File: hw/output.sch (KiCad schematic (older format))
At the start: 44 parts, among them J401 Conn_01x02, J402 Conn_01x02, J403 Conn_01x02, J404 Conn_01x02, J405 Conn_01x02, J406 Conn_01x02, J407 Conn_01x02, J408 Conn_01x02, J409 ServoCon, J410 AUDIO, Q401 IRLML6344TRPBF, Q402 IRLML6344TRPBF, Q403 IRLML6344TRPBF, Q404 CSD17306Q5A, Q406 IRLML6344TRPBF, Q408 CSD17306Q5A, U401 MCP1416, U402 MCP1416, U403 AD5160BRJZ10-R2, U404 MCP6001-OT, U405 TLP2361_TPL_E, U406 TLP2361_TPL_E

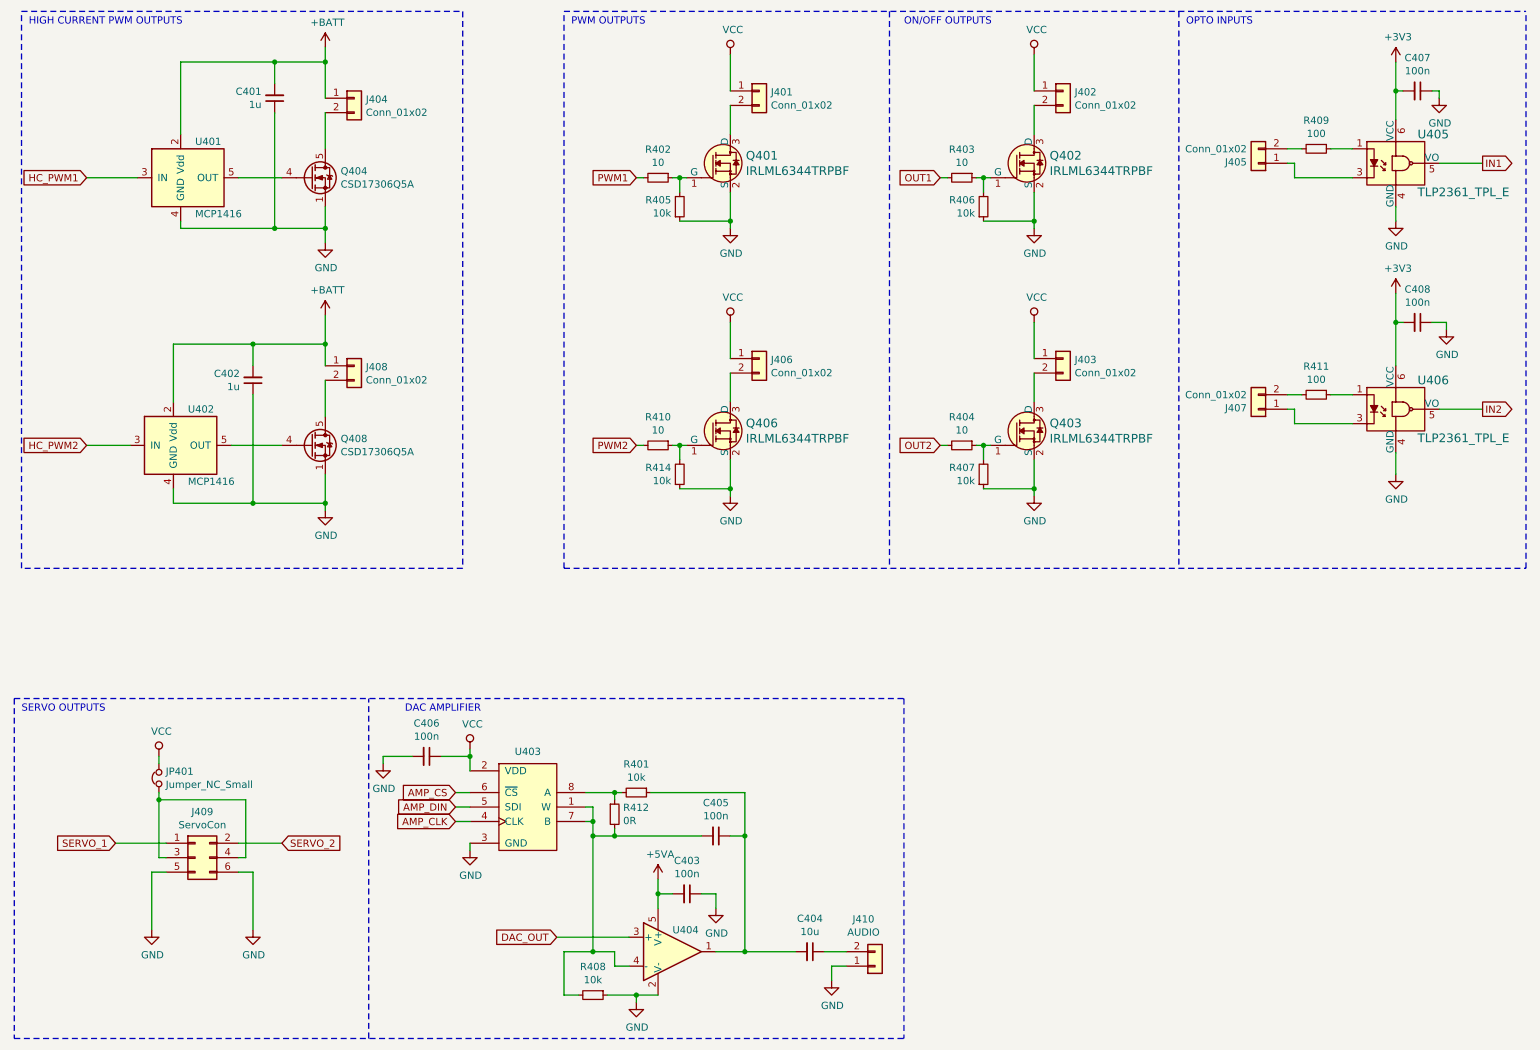
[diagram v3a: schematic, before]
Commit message: BOM Generation for 1.1 version
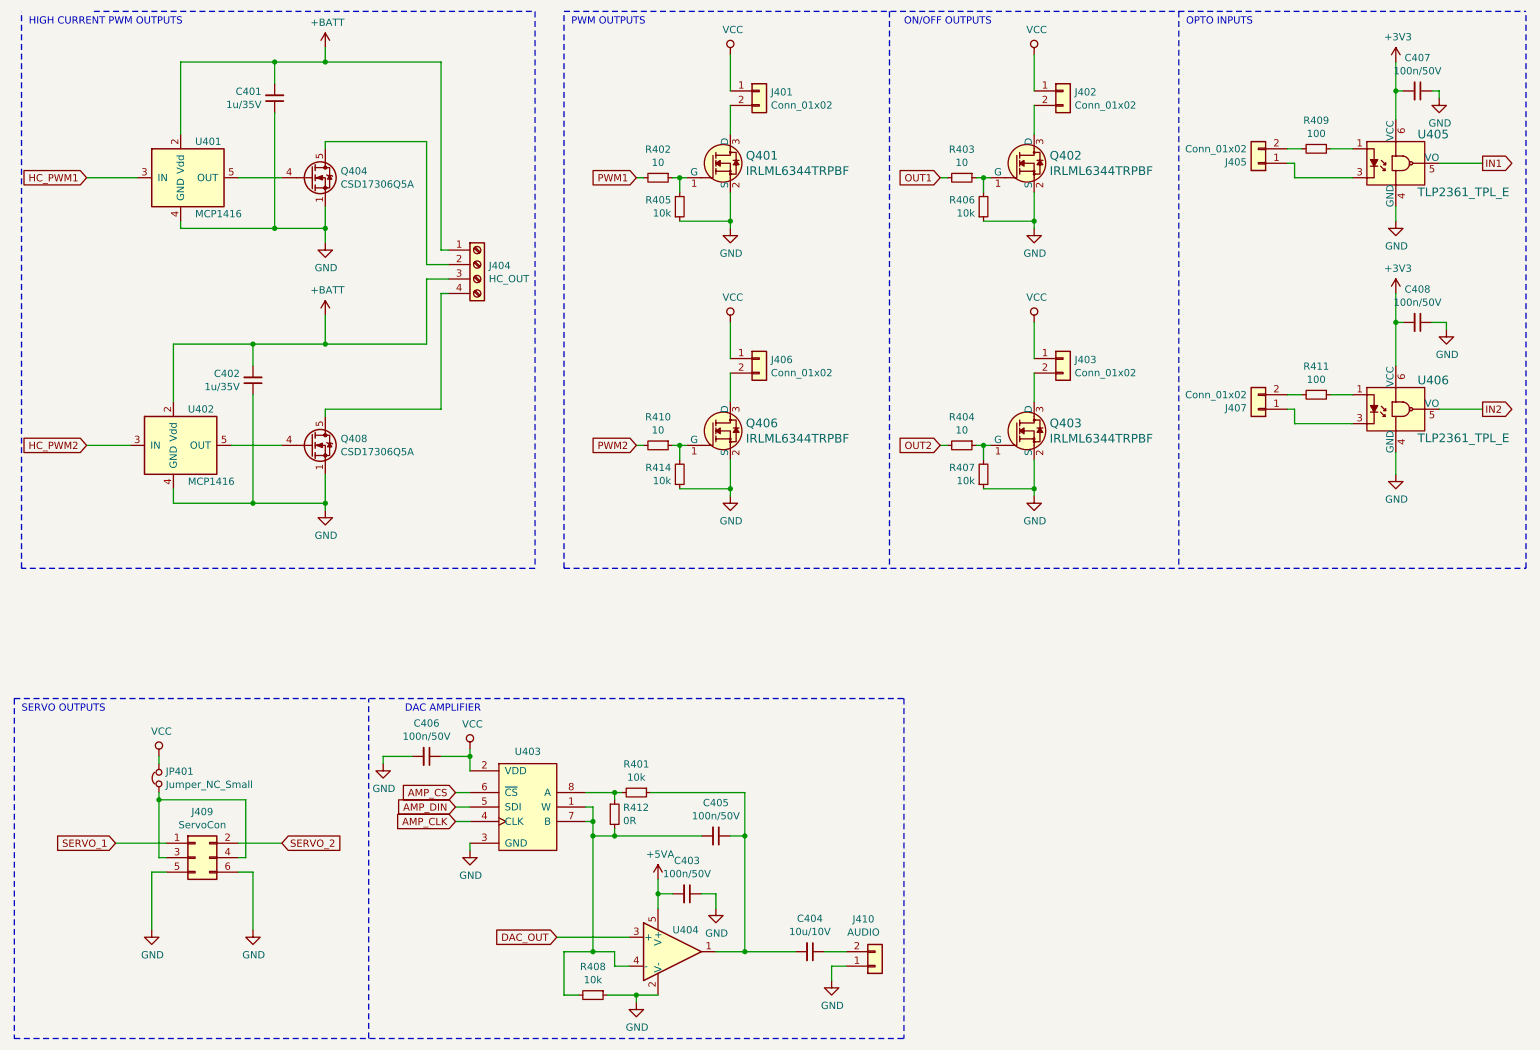
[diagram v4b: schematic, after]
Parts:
- removed J404, J408: Conn_01x02, TerminalBlock_Phoenix:TerminalBlock_Phoenix_PT-1,5-2-5.0-H_1x02_P5.00mm_Horizontal, symbol Connector_Generic:Conn_01x02
- added J404: HC_OUT, TerminalBlock_Phoenix:TerminalBlock_Phoenix_PT-1,5-4-5.0-H_1x04_P5.00mm_Horizontal, symbol Connector:Screw_Terminal_01x04
- C401, C402: value 1u -> 1u/35V
- C403, C405, C406, C407, C408: value 100n -> 100n/50V
- C404: value 10u -> 10u/10V
- J401, J402, J403, J405, J406, J407, J409, J410, JP401: Config (none) -> -prod
- Q404, Q408: MPN (none) -> CSD17306Q5A; Manufacturer (none) -> Texas Instruments
- R412: Config (none) -> dnp
- U401, U402: Description (none) -> Tiny 1.5A, High-Speed Power MOSFET DriverLo; MPN (none) -> MCP1416; Manufacturer (none) -> Microchip
- U403: Description (none) -> SPI Digital potentiometer 10k; MPN (none) -> Analog Devices; Manufacturer (none) -> AD5160BRJZ10-R2
- U404: MPN (none) -> MCP6001-OT; Manufacturer (none) -> Microchip
- U405, U406: MPN TLP2361(TPL,E -> TLP2361-TPLECT
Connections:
- net +BATT: now also J404.1 (Pin_1), J404.3 (Pin_3)
- net at Q404.5 (D): now also J404.2 (Pin_2)
- net at Q408.5 (D): now also J404.4 (Pin_4)
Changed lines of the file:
@@
 Sheet 4 4
 Title "RC Telemetry board"
-Date "2020-02-12"
-Rev "0.2"
+Date "2020-02-23"
+Rev "1.1"
 Comp "www.findersee.fi"
 Comment1 "https://github.com/findersee/rctelemetry"
@@
 	1    0    0    -1
 $EndComp
-$Comp
-L Connector_Generic:Conn_01x02 J404
-U 1 1 5CEA51F6
-P 2900 1250
-F 0 "J404" H 2980 1242 50  0000 L CNN
-F 1 "Conn_01x02" H 2980 1151 50  0000 L CNN
-F 2 "TerminalBlock_Phoenix:TerminalBlock_Phoenix_PT-1,5-2-5.0-H_1x02_P5.00mm_Horizontal" H 2900 1250 50  0001 C CNN
-F 3 "~" H 2900 1250 50  0001 C CNN
-	1    2900 1250
-	1    0    0    -1
-$EndComp
-Wire Wire Line
-	2700 1350 2700 1600
+Wire Wire Line
+	2700 1550 2700 1600
 $Comp
 L power:GND #PWR0408
@@
 	1    0    0    -1
 $EndComp
-$Comp
-L Connector_Generic:Conn_01x02 J408
-U 1 1 5CEA77CB
-P 2900 3100
-F 0 "J408" H 2980 3092 50  0000 L CNN
-F 1 "Conn_01x02" H 2980 3001 50  0000 L CNN
-F 2 "TerminalBlock_Phoenix:TerminalBlock_Phoenix_PT-1,5-2-5.0-H_1x02_P5.00mm_Horizontal" H 2900 3100 50  0001 C CNN
-F 3 "~" H 2900 3100 50  0001 C CNN
-	1    2900 3100
-	1    0    0    -1
-$EndComp
-Wire Wire Line
-	2700 3200 2700 3450
+Wire Wire Line
+	2700 3400 2700 3450
 $Comp
 L power:GND #PWR0416
@@
 F 2 "Connector_Molex:Molex_KK-254_AE-6410-02A_1x02_P2.54mm_Vertical" H 5700 1200 50  0001 C CNN
 F 3 "~" H 5700 1200 50  0001 C CNN
+F 4 "-prod" H 5700 1200 50  0001 C CNN "Config"
 	1    5700 1200
 	1    0    0    -1
@@
 F 2 "Connector_Molex:Molex_KK-254_AE-6410-02A_1x02_P2.54mm_Vertical" H 9150 1700 50  0001 C CNN
 F 3 "~" H 9150 1700 50  0001 C CNN
+F 4 "-prod" H 9150 1700 50  0001 C CNN "Config"
 	1    9150 1700
 	-1   0    0    1
@@
 F 2 "Connector_Molex:Molex_KK-254_AE-6410-02A_1x02_P2.54mm_Vertical" H 7800 1200 50  0001 C CNN
 F 3 "~" H 7800 1200 50  0001 C CNN
+F 4 "-prod" H 7800 1200 50  0001 C CNN "Config"
 	1    7800 1200
 	1    0    0    -1
@@
 F 2 "Connector_Molex:Molex_KK-254_AE-6410-02A_1x02_P2.54mm_Vertical" H 5700 3050 50  0001 C CNN
 F 3 "~" H 5700 3050 50  0001 C CNN
+F 4 "-prod" H 5700 3050 50  0001 C CNN "Config"
 	1    5700 3050
 	1    0    0    -1
@@
 F 2 "Connector_Molex:Molex_KK-254_AE-6410-02A_1x02_P2.54mm_Vertical" H 7800 3050 50  0001 C CNN
 F 3 "~" H 7800 3050 50  0001 C CNN
+F 4 "-prod" H 7800 3050 50  0001 C CNN "Config"
 	1    7800 3050
 	1    0    0    -1
@@
 F 2 "Connector_Molex:Molex_KK-254_AE-6410-02A_1x02_P2.54mm_Vertical" H 9150 3400 50  0001 C CNN
 F 3 "~" H 9150 3400 50  0001 C CNN
+F 4 "-prod" H 9150 3400 50  0001 C CNN "Config"
 	1    9150 3400
 	-1   0    0    1
@@
 F 2 "Connector_PinHeader_2.54mm:PinHeader_1x02_P2.54mm_Vertical" H 1550 5950 50  0001 C CNN
 F 3 "~" H 1550 5950 50  0001 C CNN
+F 4 "-prod" H 1550 5950 50  0001 C CNN "Config"
 	1    1550 5950
 	0    -1   -1   0
@@
 F 2 "TO_SOT_Packages_SMD:SOT-23-5_HandSoldering" H 1650 3250 50  0001 C CIN
 F 3 "http://ww1.microchip.com/downloads/en/DeviceDoc/20002092F.pdf" H 1450 3900 50  0001 C CNN
+F 4 "MCP1416" H 1650 3650 50  0001 C CNN "MPN"
+F 5 "Microchip" H 1650 3650 50  0001 C CNN "Manufacturer"
+F 6 "Tiny 1.5A, High-Speed Power MOSFET DriverLo" H 1650 3650 50  0001 C CNN "Description"
 	1    1650 3650
 	1    0    0    -1
@@
 	1650 2950 2200 2950
 Connection ~ 2700 2950
-Wire Wire Line
-	2700 2950 2700 3100
 $Comp
 L Telemetry-rescue:MCP1416-Driver_FET U401
@@
 F 2 "TO_SOT_Packages_SMD:SOT-23-5_HandSoldering" H 1700 1400 50  0001 C CIN
 F 3 "http://ww1.microchip.com/downloads/en/DeviceDoc/20002092F.pdf" H 1500 2050 50  0001 C CNN
+F 4 "MCP1416" H 1700 1800 50  0001 C CNN "MPN"
+F 5 "Microchip" H 1700 1800 50  0001 C CNN "Manufacturer"
+F 6 "Tiny 1.5A, High-Speed Power MOSFET DriverLo" H 1700 1800 50  0001 C CNN "Description"
 	1    1700 1800
 	1    0    0    -1
@@
 	1700 1000 2350 1000
 Connection ~ 2700 1000
-Wire Wire Line
-	2700 1000 2700 1250
 Wire Wire Line
 	1400 1800 1050 1800
@@
 P 2350 1250
 F 0 "C401" H 2259 1204 50  0000 R CNN
-F 1 "1u" H 2259 1295 50  0000 R CNN
+F 1 "1u/35V" H 2259 1295 50  0000 R CNN
 F 2 "Capacitor_SMD:C_0805_2012Metric_Pad1.15x1.40mm_HandSolder" H 2350 1250 50  0001 C CNN
 F 3 "~" H 2350 1250 50  0001 C CNN
@@
 P 2200 3200
 F 0 "C402" H 2109 3154 50  0000 R CNN
-F 1 "1u" H 2109 3245 50  0000 R CNN
+F 1 "1u/35V" H 2109 3245 50  0000 R CNN
 F 2 "Capacitor_SMD:C_0805_2012Metric_Pad1.15x1.40mm_HandSolder" H 2200 3200 50  0001 C CNN
 F 3 "~" H 2200 3200 50  0001 C CNN
@@
 F 2 "TO_SOT_Packages_SMD:TDSON-8-1_HandSoldering" H 2800 3575 50  0001 L CIN
 F 3 "http://www.ti.com/lit/gpn/csd17306q5a" V 2600 3650 50  0001 L CNN
+F 4 "CSD17306Q5A" H 2600 3650 50  0001 C CNN "MPN"
+F 5 "Texas Instruments" H 2600 3650 50  0001 C CNN "Manufacturer"
 	1    2600 3650
 	1    0    0    -1
@@
 F 2 "TO_SOT_Packages_SMD:TDSON-8-1_HandSoldering" H 2800 1725 50  0001 L CIN
 F 3 "http://www.ti.com/lit/gpn/csd17306q5a" V 2600 1800 50  0001 L CNN
+F 4 "CSD17306Q5A" H 2600 1800 50  0001 C CNN "MPN"
+F 5 "Texas Instruments" H 2600 1800 50  0001 C CNN "Manufacturer"
 	1    2600 1800
 	1    0    0    -1
@@
 F 2 "Connector_PinHeader_2.54mm:PinHeader_1x02_P2.54mm_Vertical" H 6500 7250 50  0001 C CNN
 F 3 "~" H 6500 7250 50  0001 C CNN
+F 4 "-prod" H 6500 7250 50  0001 C CNN "Config"
 	1    6500 7250
 	1    0    0    1
@@
 P 6050 7150
 F 0 "C404" V 5821 7150 50  0000 C CNN
-F 1 "10u" V 5912 7150 50  0000 C CNN
+F 1 "10u/10V" V 5912 7150 50  0000 C CNN
 F 2 "Capacitor_SMD:C_0603_1608Metric_Pad1.05x0.95mm_HandSolder" H 6050 7150 50  0001 C CNN
 F 3 "~" H 6050 7150 50  0001 C CNN
@@
 P 5200 6750
 F 0 "C403" V 4971 6750 50  0000 C CNN
-F 1 "100n" V 5062 6750 50  0000 C CNN
+F 1 "100n/50V" V 5062 6750 50  0000 C CNN
 F 2 "Capacitor_SMD:C_0603_1608Metric_Pad1.05x0.95mm_HandSolder" H 5200 6750 50  0001 C CNN
 F 3 "~" H 5200 6750 50  0001 C CNN
@@
 P 5400 6350
 F 0 "C405" V 5171 6350 50  0000 C CNN
-F 1 "100n" V 5262 6350 50  0000 C CNN
+F 1 "100n/50V" V 5262 6350 50  0000 C CNN
 F 2 "Capacitor_SMD:C_0603_1608Metric_Pad1.05x0.95mm_HandSolder" H 5400 6350 50  0001 C CNN
 F 3 "~" H 5400 6350 50  0001 C CNN
@@
 P 3400 5800
 F 0 "C406" V 3171 5800 50  0000 C CNN
-F 1 "100n" V 3262 5800 50  0000 C CNN
+F 1 "100n/50V" V 3262 5800 50  0000 C CNN
 F 2 "Capacitor_SMD:C_0603_1608Metric_Pad1.05x0.95mm_HandSolder" H 3400 5800 50  0001 C CNN
 F 3 "~" H 3400 5800 50  0001 C CNN
@@
 	4350 4500 4350 650
 Wire Notes Line
-	3650 650  3650 4500
-Wire Notes Line
-	3650 4500 600  4500
+	4150 650  4150 4500
+Wire Notes Line
+	4150 4500 600  4500
 Wire Notes Line
 	600  4500 600  650
 Wire Notes Line
-	600  650  3650 650
+	1100 650  4150 650
 Wire Notes Line
 	8600 650  8600 4500
@@
 F 2 "TO_SOT_Packages_SMD:SOT-23-5_HandSoldering" H 5000 6950 50  0001 L CNN
 F 3 "http://ww1.microchip.com/downloads/en/DeviceDoc/21733j.pdf" H 5100 7350 50  0001 C CNN
+F 4 "MCP6001-OT" H 5100 7150 50  0001 C CNN "MPN"
+F 5 "Microchip" H 5100 7150 50  0001 C CNN "Manufacturer"
 	1    5100 7150
 	1    0    0    -1
@@
 F 2 "Resistors_SMD:R_0402_NoSilk" H 4700 6200 50  0001 C CNN
 F 3 "~" H 4700 6200 50  0001 C CNN
+F 4 "dnp" H 4700 6200 50  0001 C CNN "Config"
 	1    4700 6200
 	1    0    0    -1
@@
 F 2 "digikey-footprints:SOT-23-8" H 3900 6100 50  0001 C CNN
 F 3 "https://www.analog.com/media/en/technical-documentation/data-sheets/AD5160.pdf" H 3900 6100 50  0001 C CNN
+F 4 "Analog Devices" H 4100 6100 50  0001 C CNN "MPN"
+F 5 "AD5160BRJZ10-R2" H 4100 6100 50  0001 C CNN "Manufacturer"
+F 6 "SPI Digital potentiometer 10k" H 4100 6100 50  0001 C CNN "Description"
 	1    4100 6100
 	1    0    0    -1
@@
 F 3 "https://toshiba.semicon-storage.com/info/docget.jsp?did=14229&prodName=TLP2361" H 10300 2000 60  0001 L CNN
 F 4 "TLP2361(TPLECT-ND" H 10300 2100 60  0001 L CNN "Digi-Key_PN"
-F 5 "TLP2361(TPL,E" H 10300 2200 60  0001 L CNN "MPN"
+F 5 "TLP2361-TPLECT" H 10300 2200 60  0001 L CNN "MPN"
 F 6 "Isolators" H 10300 2300 60  0001 L CNN "Category"
 F 7 "Optoisolators - Logic Output" H 10300 2400 60  0001 L CNN "Family"
@@
 F 3 "https://toshiba.semicon-storage.com/info/docget.jsp?did=14229&prodName=TLP2361" H 10300 3700 60  0001 L CNN
 F 4 "TLP2361(TPLECT-ND" H 10300 3800 60  0001 L CNN "Digi-Key_PN"
-F 5 "TLP2361(TPL,E" H 10300 3900 60  0001 L CNN "MPN"
+F 5 "TLP2361-TPLECT" H 10300 3900 60  0001 L CNN "MPN"
 F 6 "Isolators" H 10300 4000 60  0001 L CNN "Category"
 F 7 "Optoisolators - Logic Output" H 10300 4100 60  0001 L CNN "Family"
@@
 P 10250 1200
 F 0 "C407" V 10021 1200 50  0000 C CNN
-F 1 "100n" V 10112 1200 50  0000 C CNN
+F 1 "100n/50V" V 10112 1200 50  0000 C CNN
 F 2 "Capacitor_SMD:C_0603_1608Metric_Pad1.05x0.95mm_HandSolder" H 10250 1200 50  0001 C CNN
 F 3 "~" H 10250 1200 50  0001 C CNN
@@
 P 10250 2800
 F 0 "C408" V 10021 2800 50  0000 C CNN
-F 1 "100n" V 10112 2800 50  0000 C CNN
+F 1 "100n/50V" V 10112 2800 50  0000 C CNN
 F 2 "Capacitor_SMD:C_0603_1608Metric_Pad1.05x0.95mm_HandSolder" H 10250 2800 50  0001 C CNN
 F 3 "~" H 10250 2800 50  0001 C CNN
@@
 F 2 "Connector_PinHeader_2.54mm:PinHeader_2x03_P2.54mm_Vertical" H 1800 6500 50  0001 C CNN
 F 3 "~" H 1800 6500 50  0001 C CNN
+F 4 "-prod" H 1800 6500 50  0001 C CNN "Config"
 	1    1800 6500
 	1    0    0    -1
@@
 Text GLabel 4850 1800 0    50   Input ~ 0
 PWM1
+$Comp
+L Connector:Screw_Terminal_01x04 J404
+U 1 1 5E67202C
+P 3750 2400
+F 0 "J404" H 3830 2392 50  0000 L CNN
+F 1 "HC_OUT" H 3830 2301 50  0000 L CNN
+F 2 "TerminalBlock_Phoenix:TerminalBlock_Phoenix_PT-1,5-4-5.0-H_1x04_P5.00mm_Horizontal" H 3750 2400 50  0001 C CNN
+F 3 "~" H 3750 2400 50  0001 C CNN
+	1    3750 2400
+	1    0    0    -1
+$EndComp
+Wire Wire Line
+	3550 2300 3500 2300
+Wire Wire Line
+	3500 2300 3500 1000
+Wire Wire Line
+	3500 1000 2700 1000
+Wire Wire Line
+	2700 1550 3400 1550
+Wire Wire Line
+	3400 1550 3400 2400
+Wire Wire Line
+	3400 2400 3550 2400
+Wire Wire Line
+	2700 2950 3400 2950
+Wire Wire Line
+	3400 2950 3400 2500
+Wire Wire Line
+	3400 2500 3550 2500
+Wire Wire Line
+	3550 2600 3500 2600
+Wire Wire Line
+	3500 2600 3500 3400
+Wire Wire Line
+	3500 3400 2700 3400
 $EndSCHEMATC
